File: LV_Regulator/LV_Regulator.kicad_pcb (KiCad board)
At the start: 4 copper layers, 150 x 100 mm, 204 parts, among them IC1 UCC12040DVE, IC2 MIC29152WU, IC3 MIC29152WU, J1 430450400, J2 430450400, J3 430450800, J4 430450800, J5 SWD, J6 2169890001, K1 41.52.9.005.0010, Q1 BC807, U1 ADM2483xRW, U2 STM32F103C8Tx, U3 25CSM04xxSN, U4 BQ25858QWRRVRQ1, U5 CSD19506KTT, U6 CSD19506KTT, U7 CSD19506KTT, U8 CSD19506KTT, Y1 32.768kHz, Y2 8MHz

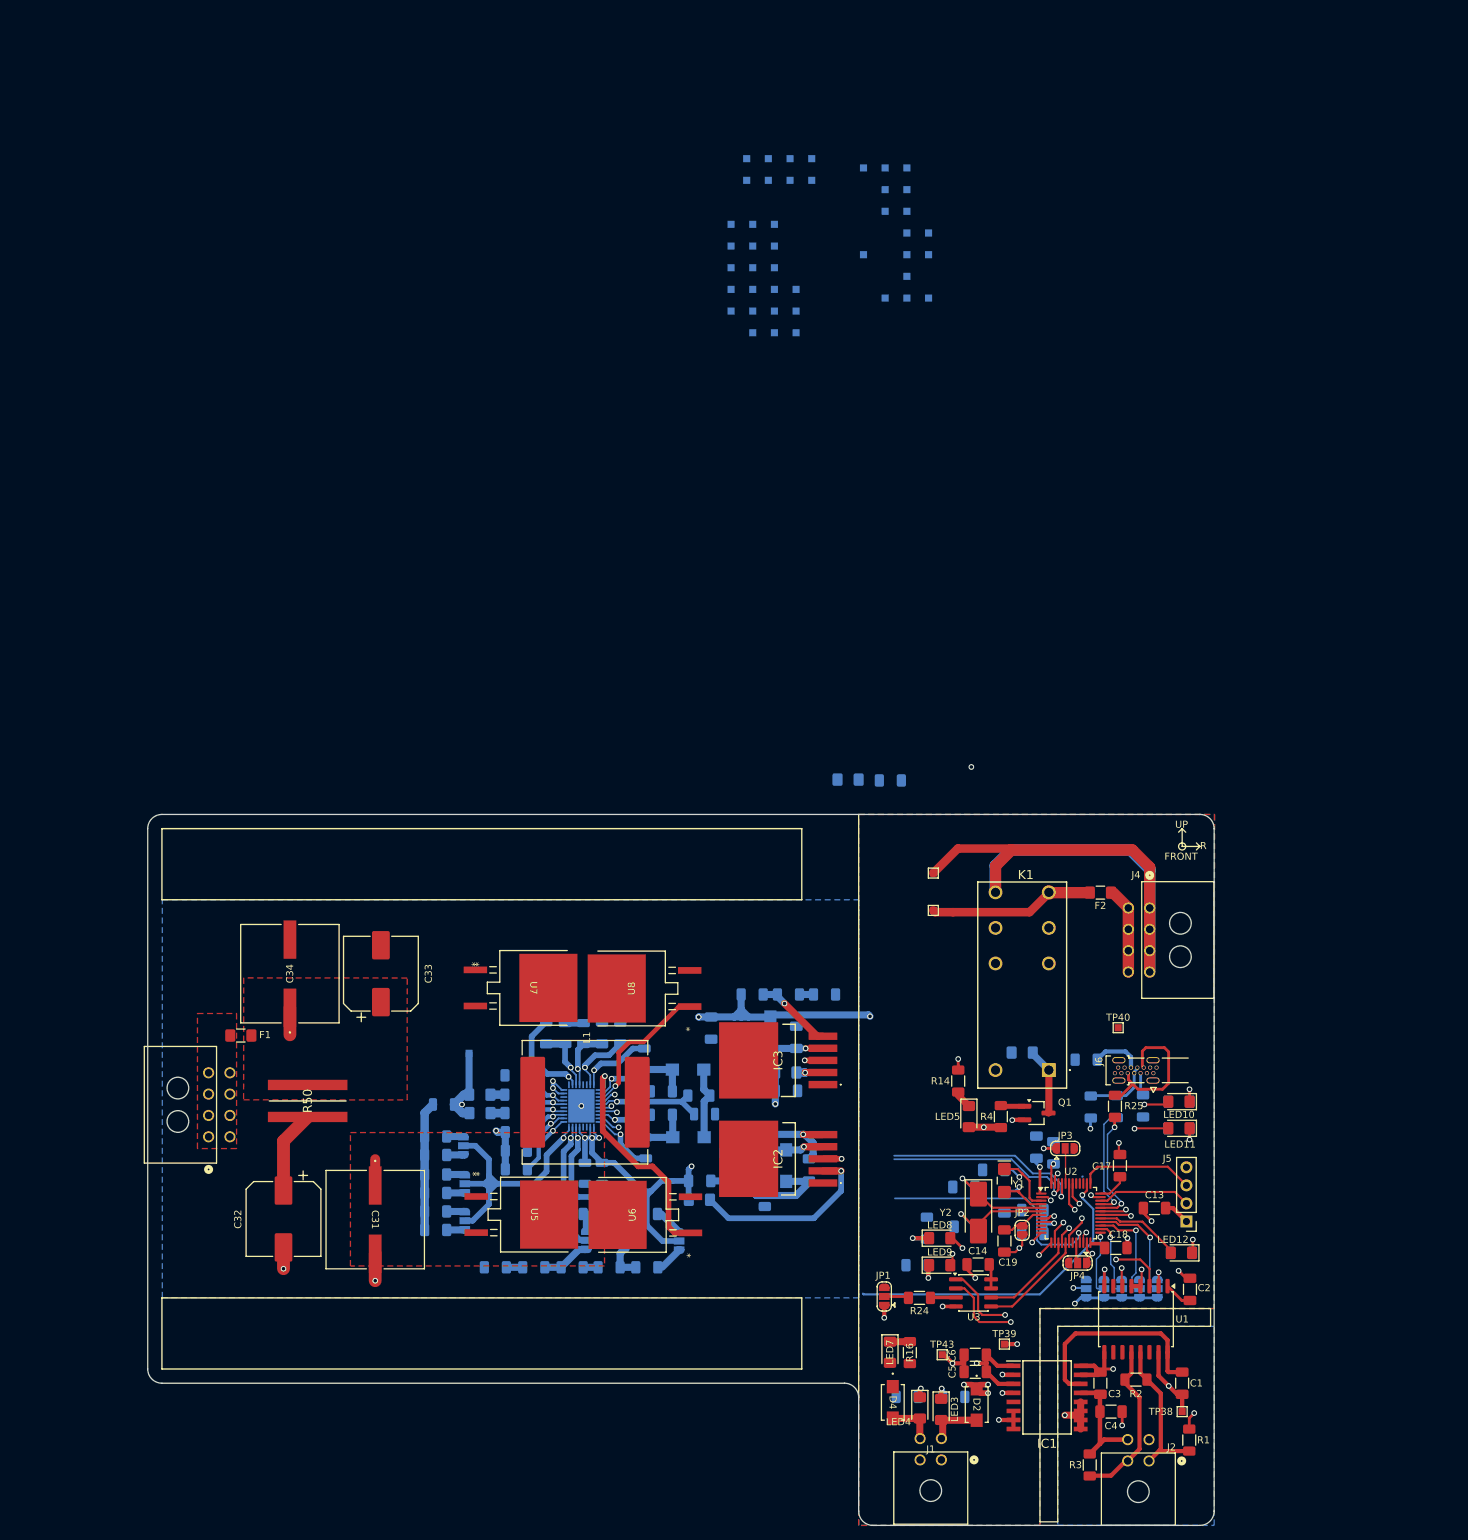
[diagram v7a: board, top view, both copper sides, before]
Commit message: Major PCB Routing Progress
Finished routing of all Regulator & Power components and connections.
Also routed & placed a good amount of power electronics side TP's, only a few left which are Logic Supply TP's and the MCU side TP's.
Only Routing on the Power side left are  the few remaining test points.

Additional detail, removed all Teardrops because of their deletion residue, in doing so, I've also removed all the residue.
Tear drops will be added after final routing for the revision has been finished.
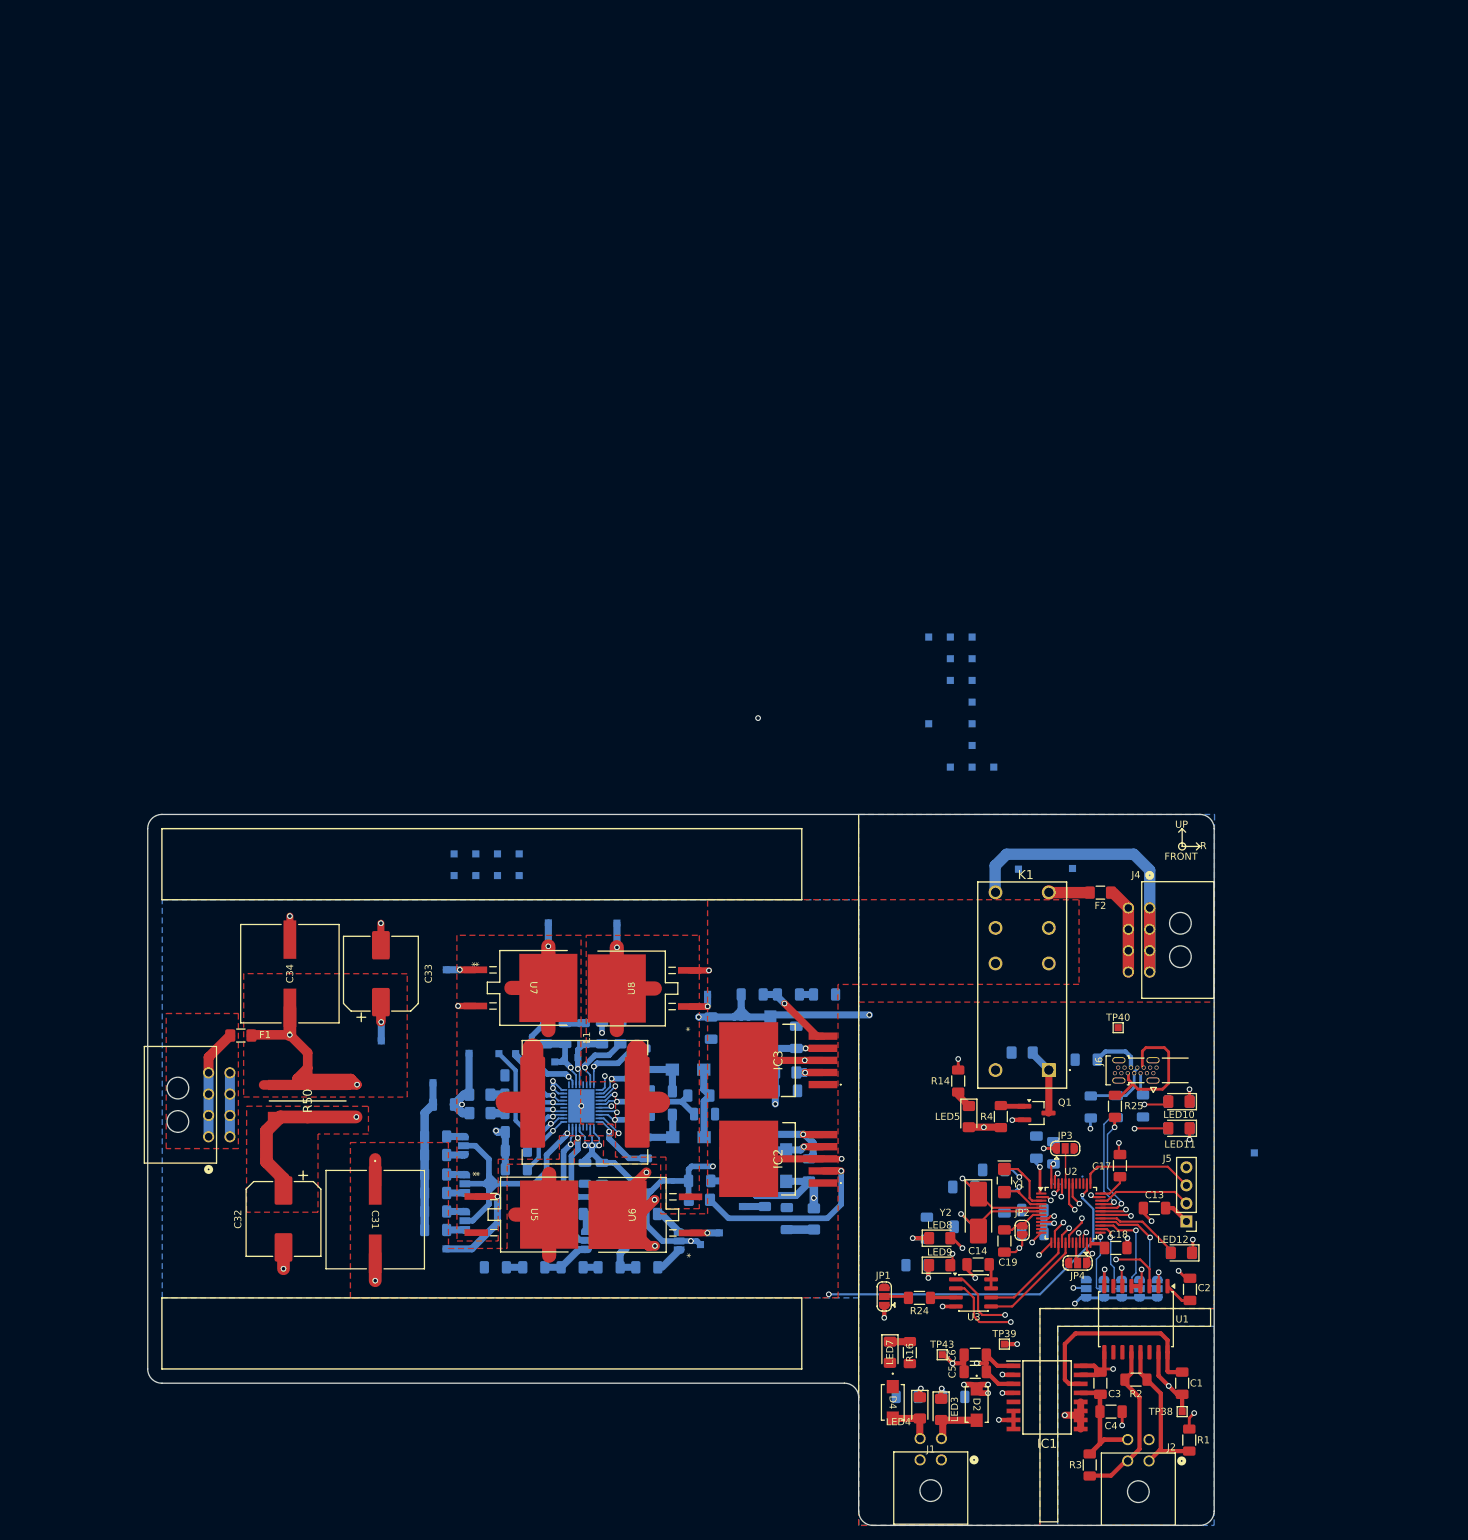
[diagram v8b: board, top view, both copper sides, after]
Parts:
- TP4, TP51: moved to B.Cu
- moved TP31 139.8 mm to (123.0, 105.1)
- moved TP8 138.7 mm to (137.7, 97.4)
- moved TP44 137.5 mm to (236.7, 91.6)
- moved TP14 136.3 mm to (134.4, 99.7)
- moved TP7 134.6 mm to (147.7, 97.8)
- moved TP2 131.4 mm to (158.8, 104.5)
- moved TP13 131.2 mm to (134.4, 97.5)
- moved TP36 127.5 mm to (149.1, 87.0)
- moved TP5 127.1 mm to (108.7, 82.0)
- moved TP30 126.8 mm to (161.4, 102.8)
- moved TP29 126.0 mm to (141.5, 78.2)
- moved TP28 125.1 mm to (138.2, 78.8)
- moved TP41 123.1 mm to (164.7, 99.2)
- moved TP27 121.3 mm to (132.8, 77.7)
- moved TP42 120.0 mm to (121.1, 81.7)
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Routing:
- net INT_N: track 39.7 -> 117.6 mm
- net CE_N: track 51.3 -> 116.7 mm, vias 2 -> 3
- net LODRV1_FET2: track 2.58 -> 56.4 mm, vias 1 -> 2
- net I2C_SDA: track 34.3 -> 87.3 mm
- net VOUT: track 17.4 -> 67.9 mm, vias 1 -> 4
- net I2C_SCL: track 37.7 -> 87.9 mm
- net BAT-: track 96.6 -> 50.4 mm
- net GND: track 93.2 -> 138.3 mm, vias 29 -> 33
- net HIDRV1_FET1: track 3.29 -> 43.4 mm, vias 1 -> 2
- net Net-(U6-D): track 11.8 -> 45.2 mm, vias 0 -> 5
- net SW1: track 9.51 -> 41.0 mm, vias 1 -> 2
- net SW2: track 10.4 -> 41.5 mm, vias 1 -> 2
- net SYS: track 71.0 -> 91.9 mm, vias 5 -> 6
- net BAT+: track 22.8 -> 5.35 mm
- net Net-(F1-Pad2): track 0.00 -> 15.5 mm
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- added copper zone on F.Cu, net Net-(U6-D)
- added copper zone on In2.Cu, net Net-(U6-D)
- added copper zone on F.Cu, net SW1
- added copper zone on F.Cu, net SW2
- added copper zone on In2.Cu, net VOUT
- removed copper zone on In2.Cu, net GND
- removed copper zone on In1.Cu, net VOUT
